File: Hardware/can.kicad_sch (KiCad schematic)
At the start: 11 parts, among them U20 SN65HVD230

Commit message: fixes
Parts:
- removed C53, C54: DNP, Capacitor_SMD:C_0402_1005Metric, symbol Device:C_Small
- JP3: footprint Jumper:SolderJumper-2_P1.3mm_Open_RoundedPad1.0x1.5mm -> iclr-hw:SmallerSolderJP
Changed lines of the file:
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@@
-	(wire
-		(pts
-			(xy 175.26 85.09) (xy 175.26 88.9)
-		)
-		(stroke
-			(width 0)
-			(type default)
-		)
-	)
 	(wire
 		(pts
@@
 	)
 	(symbol
-		(lib_id "Device:C_Small")
-		(at 175.26 82.55 180)
-		(unit 1)
-		(exclude_from_sim no)
-		(in_bom yes)
-		(on_board yes)
-		(dnp no)
-		(property "Reference" "C53"
-			(at 173.99 74.93 0)
-			(effects
-				(font
-					(size 1.27 1.27)
-				)
-				(justify right)
-			)
-		)
-		(property "Value" "DNP"
-			(at 173.99 77.47 0)
-			(effects
-				(font
-					(size 1.27 1.27)
-				)
-				(justify right)
-			)
-		)
-		(property "Footprint" "Capacitor_SMD:C_0402_1005Metric"
-			(at 175.26 82.55 0)
-			(effects
-				(font
-					(size 1.27 1.27)
-				)
-				(hide yes)
-			)
-		)
-		(property "Datasheet" "~"
-			(at 175.26 82.55 0)
-			(effects
-				(font
-					(size 1.27 1.27)
-				)
-				(hide yes)
-			)
-		)
-		(property "Description" ""
-			(at 175.26 82.55 0)
-			(effects
-				(font
-					(size 1.27 1.27)
-				)
-				(hide yes)
-			)
-		)
-		(pin "1"
-		)
-		(pin "2"
-		)
-		(instances
-			(project "PickleRick"
-				(path "/e63e39d7-6ac0-4ffd-8aa3-1841a4541b55/84dc3251-c581-43e1-8e86-e53b5efc8269"
-					(reference "C53")
-					(unit 1)
-				)
-			)
-		)
-	)
-	(symbol
 		(lib_id "Diode:SM712_SOT23")
 		(at 186.69 88.9 270)
@@
 	)
 	(symbol
-		(lib_id "power:GND")
-		(at 175.26 102.87 0)
-		(unit 1)
-		(exclude_from_sim no)
-		(in_bom yes)
-		(on_board yes)
-		(dnp no)
-		(fields_autoplaced yes)
-		(property "Reference" "#PWR0125"
-			(at 175.26 109.22 0)
-			(effects
-				(font
-					(size 1.27 1.27)
-				)
-				(hide yes)
-			)
-		)
-		(property "Value" "GND"
-			(at 175.26 106.68 0)
-			(effects
-				(font
-					(size 1.27 1.27)
-				)
-			)
-		)
-		(property "Footprint" ""
-			(at 175.26 102.87 0)
-			(effects
-				(font
-					(size 1.27 1.27)
-				)
-				(hide yes)
-			)
-		)
-		(property "Datasheet" ""
-			(at 175.26 102.87 0)
-			(effects
-				(font
-					(size 1.27 1.27)
-				)
-				(hide yes)
-			)
-		)
-		(property "Description" ""
-			(at 175.26 102.87 0)
-			(effects
-				(font
-					(size 1.27 1.27)
-				)
-				(hide yes)
-			)
-		)
-		(pin "1"
-		)
-		(instances
-			(project "PickleRick"
-				(path "/e63e39d7-6ac0-4ffd-8aa3-1841a4541b55/84dc3251-c581-43e1-8e86-e53b5efc8269"
-					(reference "#PWR0125")
-					(unit 1)
-				)
-			)
-		)
-	)
-	(symbol
 		(lib_id "Device:C_Small")
 		(at 121.92 71.12 0)
@@
 			)
 		)
-		(property "Footprint" "Jumper:SolderJumper-2_P1.3mm_Open_RoundedPad1.0x1.5mm"
+		(property "Footprint" "iclr-hw:SmallerSolderJP"
 			(at 157.48 88.9 0)
 			(effects
@@
 					(unit 1)
 				)
-			)
-		)
-	)
-	(symbol
-		(lib_id "Device:C_Small")
-		(at 175.26 100.33 180)
-		(unit 1)
-		(exclude_from_sim no)
-		(in_bom yes)
-		(on_board yes)
-		(dnp no)
-		(fields_autoplaced yes)
-		(property "Reference" "C54"
-			(at 177.8 99.0535 0)
-			(effects
-				(font
-					(size 1.27 1.27)
-				)
-				(justify right)
-			)
-		)
-		(property "Value" "DNP"
-			(at 177.8 101.5935 0)
-			(effects
-				(font
-					(size 1.27 1.27)
-				)
-				(justify right)
-			)
-		)
-		(property "Footprint" "Capacitor_SMD:C_0402_1005Metric"
-			(at 175.26 100.33 0)
-			(effects
-				(font
-					(size 1.27 1.27)
-				)
-				(hide yes)
-			)
-		)
-		(property "Datasheet" "~"
-			(at 175.26 100.33 0)
-			(effects
-				(font
-					(size 1.27 1.27)
-				)
-				(hide yes)
-			)
-		)
-		(property "Description" ""
-			(at 175.26 100.33 0)
-			(effects
-				(font
-					(size 1.27 1.27)
-				)
-				(hide yes)
-			)
-		)
-		(pin "1"
-		)
-		(pin "2"
-		)
-		(instances
-			(project "PickleRick"
-				(path "/e63e39d7-6ac0-4ffd-8aa3-1841a4541b55/84dc3251-c581-43e1-8e86-e53b5efc8269"
-					(reference "C54")
-					(unit 1)
-				)

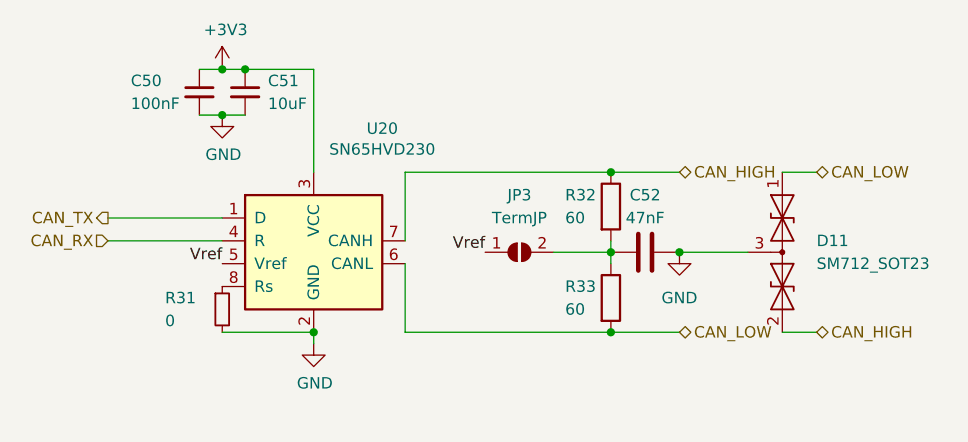
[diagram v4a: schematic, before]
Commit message: Updated Baseboard design but with power supply problems
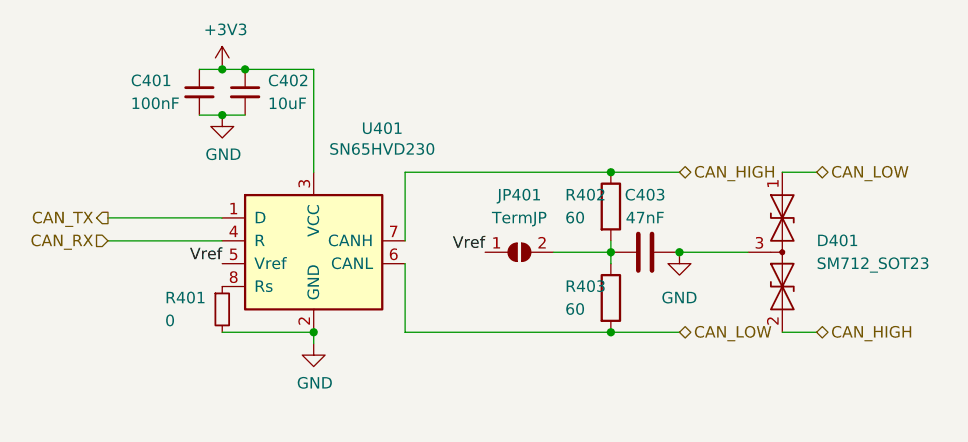
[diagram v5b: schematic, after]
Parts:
- renumbered C50 to C401, C51 to C402, C52 to C403, D11 to D401, JP3 to JP401, R31 to R401, R32 to R402, R33 to R403, U20 to U401
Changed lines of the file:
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@@
 (kicad_sch
-	(version 20231120)
+	(version 20250114)
 	(generator "eeschema")
-	(generator_version "8.0")
+	(generator_version "9.0")
 	(paper "A4")
 	(junction
@@
 		(dnp no)
 		(fields_autoplaced yes)
-		(property "Reference" "#PWR0123"
+		(property "Reference" "#PWR0403"
 			(at 134.62 105.41 0)
 			(effects
@@
 			(project "PickleRick"
 				(path "/e63e39d7-6ac0-4ffd-8aa3-1841a4541b55/84dc3251-c581-43e1-8e86-e53b5efc8269"
-					(reference "#PWR0123")
+					(reference "#PWR0403")
 					(unit 1)
 				)
@@
 		(dnp no)
 		(fields_autoplaced yes)
-		(property "Reference" "#PWR0121"
+		(property "Reference" "#PWR0401"
 			(at 124.46 72.39 0)
 			(effects
@@
 			(project "PickleRick"
 				(path "/e63e39d7-6ac0-4ffd-8aa3-1841a4541b55/84dc3251-c581-43e1-8e86-e53b5efc8269"
-					(reference "#PWR0121")
+					(reference "#PWR0401")
 					(unit 1)
 				)
@@
 		(dnp no)
 		(fields_autoplaced yes)
-		(property "Reference" "U20"
+		(property "Reference" "U401"
 			(at 142.24 75.1586 0)
 			(effects
@@
 			(project "PickleRick"
 				(path "/e63e39d7-6ac0-4ffd-8aa3-1841a4541b55/84dc3251-c581-43e1-8e86-e53b5efc8269"
-					(reference "U20")
+					(reference "U401")
 					(unit 1)
 				)
@@
 		(dnp no)
 		(fields_autoplaced yes)
-		(property "Reference" "C51"
+		(property "Reference" "C402"
 			(at 129.54 69.8562 0)
 			(effects
@@
 			(project "PickleRick"
 				(path "/e63e39d7-6ac0-4ffd-8aa3-1841a4541b55/84dc3251-c581-43e1-8e86-e53b5efc8269"
-					(reference "C51")
+					(reference "C402")
 					(unit 1)
 				)
@@
 		(dnp no)
 		(fields_autoplaced yes)
-		(property "Reference" "D11"
+		(property "Reference" "D401"
 			(at 190.5 87.63 90)
 			(effects
@@
 			(project "PickleRick"
 				(path "/e63e39d7-6ac0-4ffd-8aa3-1841a4541b55/84dc3251-c581-43e1-8e86-e53b5efc8269"
-					(reference "D11")
+					(reference "D401")
 					(unit 1)
 				)
@@
 		(dnp no)
 		(fields_autoplaced yes)
-		(property "Reference" "#PWR0124"
+		(property "Reference" "#PWR0404"
 			(at 175.26 95.25 0)
 			(effects
@@
 			(project "PickleRick"
 				(path "/e63e39d7-6ac0-4ffd-8aa3-1841a4541b55/84dc3251-c581-43e1-8e86-e53b5efc8269"
-					(reference "#PWR0124")
+					(reference "#PWR0404")
 					(unit 1)
 				)
@@
 		(dnp no)
 		(fields_autoplaced yes)
-		(property "Reference" "C50"
+		(property "Reference" "C401"
 			(at 114.3 69.85 0)
 			(effects
@@
 			(project "PickleRick"
 				(path "/e63e39d7-6ac0-4ffd-8aa3-1841a4541b55/84dc3251-c581-43e1-8e86-e53b5efc8269"
-					(reference "C50")
+					(reference "C401")
 					(unit 1)
 				)
@@
 		(on_board yes)
 		(dnp no)
-		(property "Reference" "R31"
+		(property "Reference" "R401"
 			(at 118.11 93.98 0)
 			(effects
@@
 			(project "PickleRick"
 				(path "/e63e39d7-6ac0-4ffd-8aa3-1841a4541b55/84dc3251-c581-43e1-8e86-e53b5efc8269"
-					(reference "R31")
+					(reference "R401")
 					(unit 1)
 				)
@@
 		(dnp no)
 		(fields_autoplaced yes)
-		(property "Reference" "R33"
+		(property "Reference" "R403"
 			(at 162.56 92.71 0)
 			(effects
@@
 			(project "PickleRick"
 				(path "/e63e39d7-6ac0-4ffd-8aa3-1841a4541b55/84dc3251-c581-43e1-8e86-e53b5efc8269"
-					(reference "R33")
+					(reference "R403")
 					(unit 1)
 				)
@@
 		(dnp no)
 		(fields_autoplaced yes)
-		(property "Reference" "R32"
+		(property "Reference" "R402"
 			(at 162.56 82.55 0)
 			(effects
@@
 			(project "PickleRick"
 				(path "/e63e39d7-6ac0-4ffd-8aa3-1841a4541b55/84dc3251-c581-43e1-8e86-e53b5efc8269"
-					(reference "R32")
+					(reference "R402")
 					(unit 1)
 				)
@@
 		(dnp no)
 		(fields_autoplaced yes)
-		(property "Reference" "C52"
+		(property "Reference" "C403"
 			(at 171.45 82.55 90)
 			(effects
@@
 			(project "PickleRick"
 				(path "/e63e39d7-6ac0-4ffd-8aa3-1841a4541b55/84dc3251-c581-43e1-8e86-e53b5efc8269"
-					(reference "C52")
+					(reference "C403")
 					(unit 1)
 				)
@@
 		(dnp no)
 		(fields_autoplaced yes)
-		(property "Reference" "#PWR0122"
+		(property "Reference" "#PWR0402"
 			(at 124.46 80.01 0)
 			(effects
@@
 			(project "PickleRick"
 				(path "/e63e39d7-6ac0-4ffd-8aa3-1841a4541b55/84dc3251-c581-43e1-8e86-e53b5efc8269"
-					(reference "#PWR0122")
+					(reference "#PWR0402")
 					(unit 1)
 				)
@@
 		(dnp no)
 		(fields_autoplaced yes)
-		(property "Reference" "JP3"
+		(property "Reference" "JP401"
 			(at 157.48 82.55 0)
 			(effects
@@
 			(project "PickleRick"
 				(path "/e63e39d7-6ac0-4ffd-8aa3-1841a4541b55/84dc3251-c581-43e1-8e86-e53b5efc8269"
-					(reference "JP3")
-					(unit 1)
-				)
+					(reference "JP401")
+					(unit 1)
+				)
